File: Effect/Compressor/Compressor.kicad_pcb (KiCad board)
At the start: 2 copper layers, 30 x 62 mm, 34 parts, among them J1 Conn_01x04_Pin, J2 Conn_01x04_Pin, Q1 MMBF5103, Q2 DMMT5551, Q3 MMBF5103

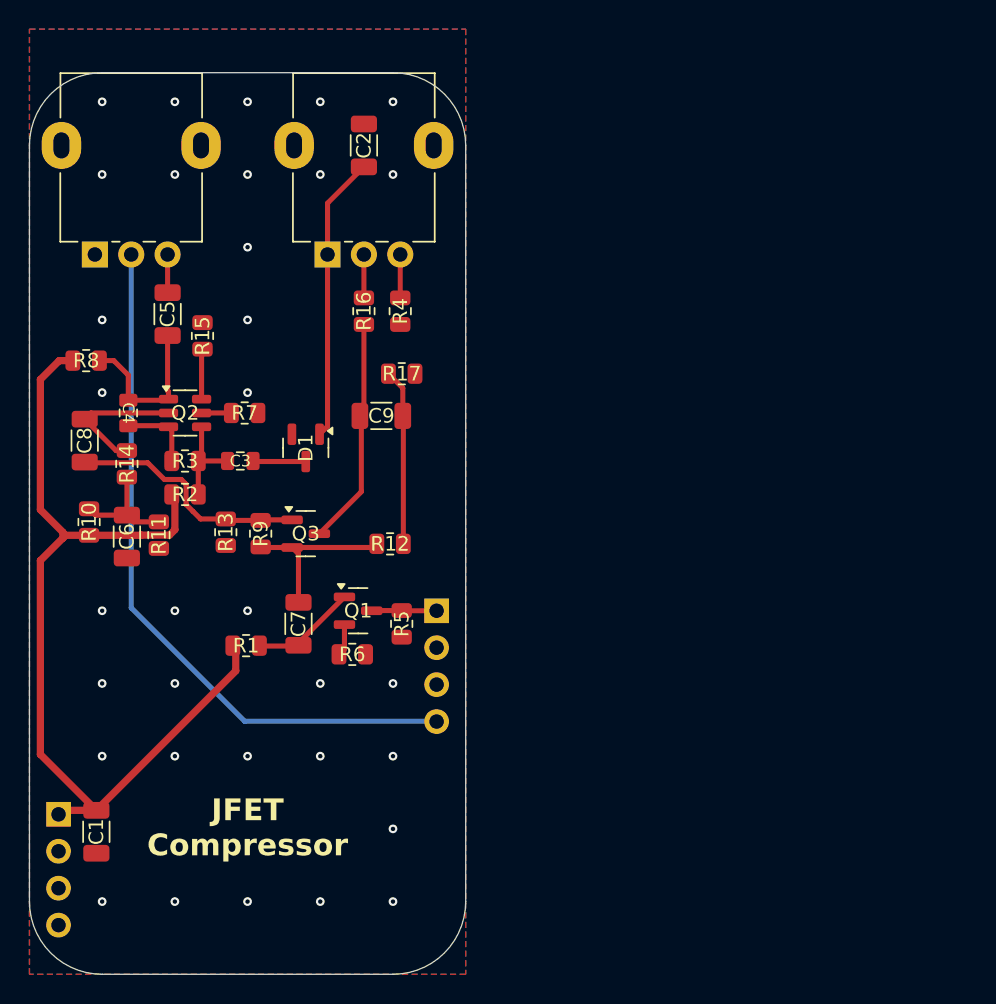
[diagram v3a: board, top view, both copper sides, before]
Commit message: More compressor updates: add pots for attack / decay tuning etc
Lots of minor changes, but the user-visible one is that there is
(limited) control of the attack and delay now.  But the whole compressor
level setup has also changed, and the signal amplification is done a bit
differently too using the NPN/PNP pair in the NMB2227A.

Can you say "trying out random things"? I knew you could.

Let's get this manufactured and see if it actually works, since I won't
have time to mess with the design any more as the merge window opens and
my travel season starts.

Signed-off-by: Linus Torvalds <torvalds@linux-foundation.org>
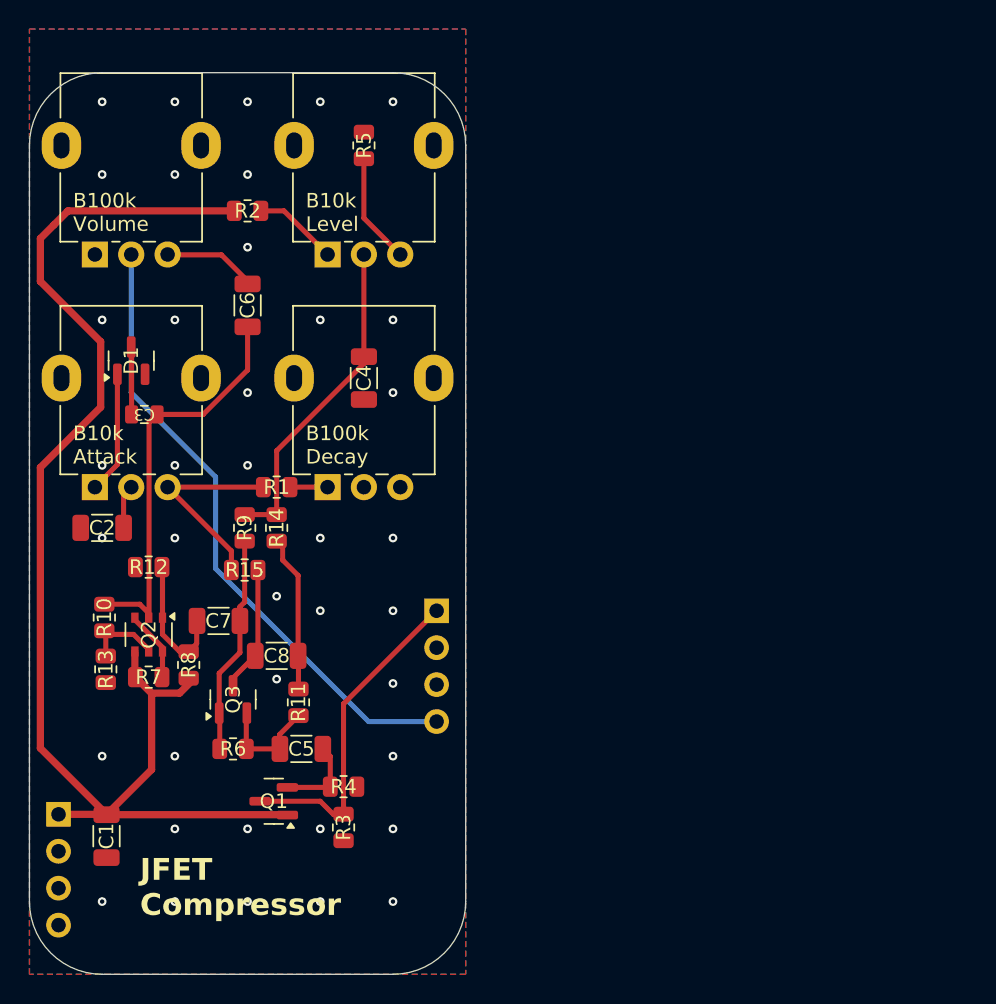
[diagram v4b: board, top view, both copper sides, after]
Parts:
- removed the C6 at (91.7, 94.9)
- removed the R11 at (93.9, 94.8)
- removed the R14 at (91.7, 89.9)
- removed the R3 at (95.7, 89.7)
- removed the R4 at (110.5, 79.4)
- removed the R8 at (88.9, 82.8)
- added R10: 2k2, Resistor_SMD:R_0805_2012Metric, F.Cu at (90.2, 100.5)
- added R12: 10k, Resistor_SMD:R_0805_2012Metric, F.Cu at (93.2, 97.0)
- added R5: 2k2, Resistor_SMD:R_0805_2012Metric, F.Cu at (108.0, 68.0)
- added RV2: 100k Decay, Mylib:Potentiometer_9mm_MP, F.Cu at (108.0, 84.0)
- added RV3: 10k Level, Mylib:Potentiometer_9mm_MP, F.Cu at (108.0, 68.0)
- C2: value 1uF -> 0.22uF
- C4: value 0.1uF -> 22uF; footprint Mylib:C_0704_1810Metric -> Capacitor_SMD:C_1206_3216Metric
- C5: renamed from C7; value 1uF -> 4.7uF
- C6: renamed from C5; value 1uF -> 4.7uF
- C7: renamed from C8; value 1uF -> 4.7uF
- Q2: value DMMT5551 -> NMB2227A; footprint Package_TO_SOT_SMD:SOT-23-6 -> Package_SO:TSOP-6_1.65x3.05mm_P0.95mm
- R1: value 1k5 -> 100k
- R13: renamed from R15; value 3k3 -> 1k
- R2: value 10k -> 33k
- R4: renamed from R6; value 1k -> 2k2
- R6: renamed from R9; value 33k -> 180k
- R7: value 3k3 -> 620
- R8: renamed from R10; value 100k -> 39k
- RV1: value 100k -> 10k Attack
- RV4: renamed from RV2; value 100k -> 100k Volume
- moved C2 31.9 mm to (90.0, 94.3), turned to 180 degrees
- moved R13 23.9 mm to (90.2, 104.0), turned to -90 degrees
- moved RV1 22.6 mm to (92.0, 84.0)
- moved R2 20.0 mm to (100.0, 72.5), turned to 180 degrees
- moved R15 19.6 mm to (99.8, 97.2), turned to 0 degrees
- moved R7 19.3 mm to (93.2, 104.6)
- moved C8 18.0 mm to (102.0, 103.1)
- moved C4 16.4 mm to (108.0, 84.0)
- moved Q2 15.4 mm to (93.2, 101.6), turned to -90 degrees
- moved C7 15.4 mm to (98.0, 100.7), turned to 180 degrees
- moved R6 14.9 mm to (99.0, 109.5), turned to 180 degrees
- moved R3 14.6 mm to (106.6, 114.9)
- moved Q1 14.3 mm to (101.8, 113.1), turned to 180 degrees
- moved R14 13.6 mm to (102.0, 94.3), turned to 90 degrees
- moved D1 13.4 mm to (92.0, 82.8), turned to 90 degrees
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- renumbered C9 to C8, R12 to R11, R17 to R14, R16 to R15, R5 to R3, R13 to R9
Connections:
- net Net-(Q3-D) renamed AMP_IN
- C2 pad 1: RECT -> Net-(C2-Pad1)
- C3 pad 1: Net-(Q2B-C) -> AMP_OUT
- C4 pad 1: FB -> LEVEL
- C4 pad 2: Net-(Q2B-B) -> GND
- C6 pad 1: FB -> AMP_OUT
- C7 pad 2: Net-(Q2A-B) -> Net-(Q2A-B1)
- D1 pad 1: RECT -> Net-(D1-A)
- Q1 pad 1: BUF_IN -> +V
- Q1 pad 2: Net-(Q1-S) -> BUF_IN
- Q2 pad 1: FB -> Net-(Q2A-B1)
- Q2 pad 2: Net-(Q2A-B) -> AMP_OUT
- Q2 pad 3: Net-(Q2B-B) -> Net-(Q2A-C1)
- Q2 pad 4: Net-(Q2B-C) -> +V
- Q2 pad 5: Net-(Q2B-E) -> Net-(Q2A-E1)
- Q2 pad 6: Net-(Q2A-E) -> Net-(Q2A-C1)
- R1 pad 1: +V -> Net-(R1-Pad1)
- R1 pad 2: BUF_IN -> RECT
- R13 pad 1: Net-(Q2A-E) -> Net-(Q2A-E1)
- R14 pad 2: GND -> LEVEL
- R15 pad 1: CONTROL -> RECT
- R2 pad 1: +V -> Net-(R2-Pad1)
- R2 pad 2: Net-(Q2B-C) -> +V
- R4 pad 1: Net-(Q1-S) -> BUF_IN
- R7 pad 1: Net-(Q2B-E) -> +V
- R7 pad 2: GND -> Net-(Q2A-C1)
- R8 pad 1: VBIAS -> Net-(Q2A-B1)
- R9 pad 2: GND -> LEVEL
- RV1 pad 1: RECT -> Net-(D1-A)
- RV1 pad 2: CONTROL -> Net-(C2-Pad1)
- RV1 pad 3: Net-(R4-Pad2) -> RECT
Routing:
- net AMP_OUT: track 0.00 -> 28.2 mm
- net +V: track 63.8 -> 91.1 mm
- net LEVEL: track 0.00 -> 22.6 mm
- net IN: track 4.47 -> 22.8 mm
- net FB: track 11.3 -> 0.00 mm
- net Net-(Q2A-B): track 9.73 -> 0.00 mm
- net Net-(Q2A-B1): track 0.00 -> 9.39 mm
- net Net-(D1-A): track 0.00 -> 8.40 mm
- net VBIAS: track 7.79 -> 0.00 mm
- net Net-(R5-Pad2): track 0.00 -> 7.62 mm
- net Net-(Q3-G): track 15.7 -> 8.67 mm
- net Net-(Q2B-C): track 6.76 -> 0.00 mm
- net Net-(R2-Pad1): track 0.00 -> 5.83 mm
- net RECT: track 19.7 -> 14.1 mm
- net Net-(Q2A-E1): track 0.00 -> 5.36 mm
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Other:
- board text added: "B100k Decay"
- board text added: "B100k Volume"
- board text added: "B10k Attack"
- board text added: "B10k Level"

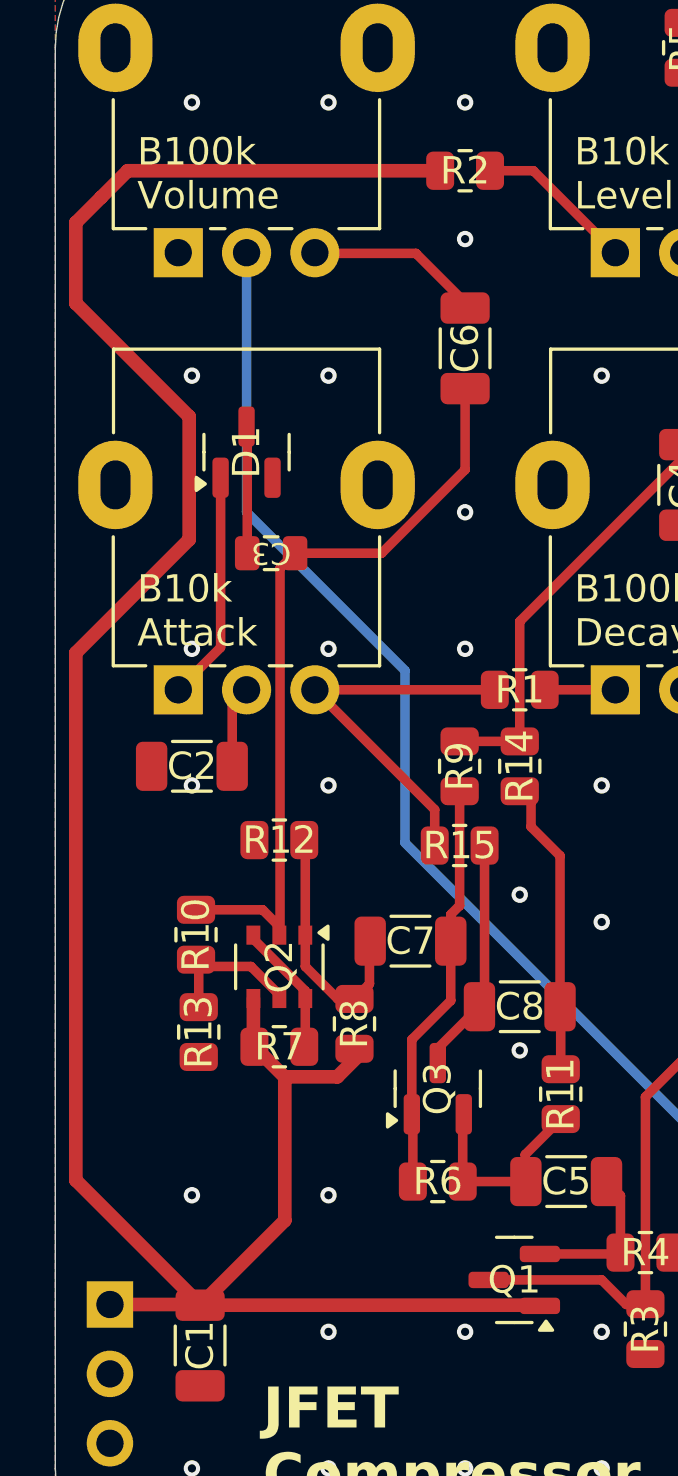
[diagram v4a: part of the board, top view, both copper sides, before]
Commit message: Gaah - Fix stupid PNP direction mistake
I've done this *so* many times: I turn the PNP around by rotating it
like it's some random resistor, not my mirroring it around the Y-axis,
and I end up with the transistor the wrong way around without noticing
it.

And I did it *again*.

It didn't actually seem to matter for simulation, because this whole
"use a series pair" was just for the lulz and there wasn't any big
current or voltage gain expected.  And so the single NPN was perfectly
happy to drive it all.

But it's still very wrong indeed.

This just fixes the direction of the transistor, but I'll go look closer
if it had some unfortunate effect on the rest of my flawed results.

Signed-off-by: Linus Torvalds <torvalds@linux-foundation.org>
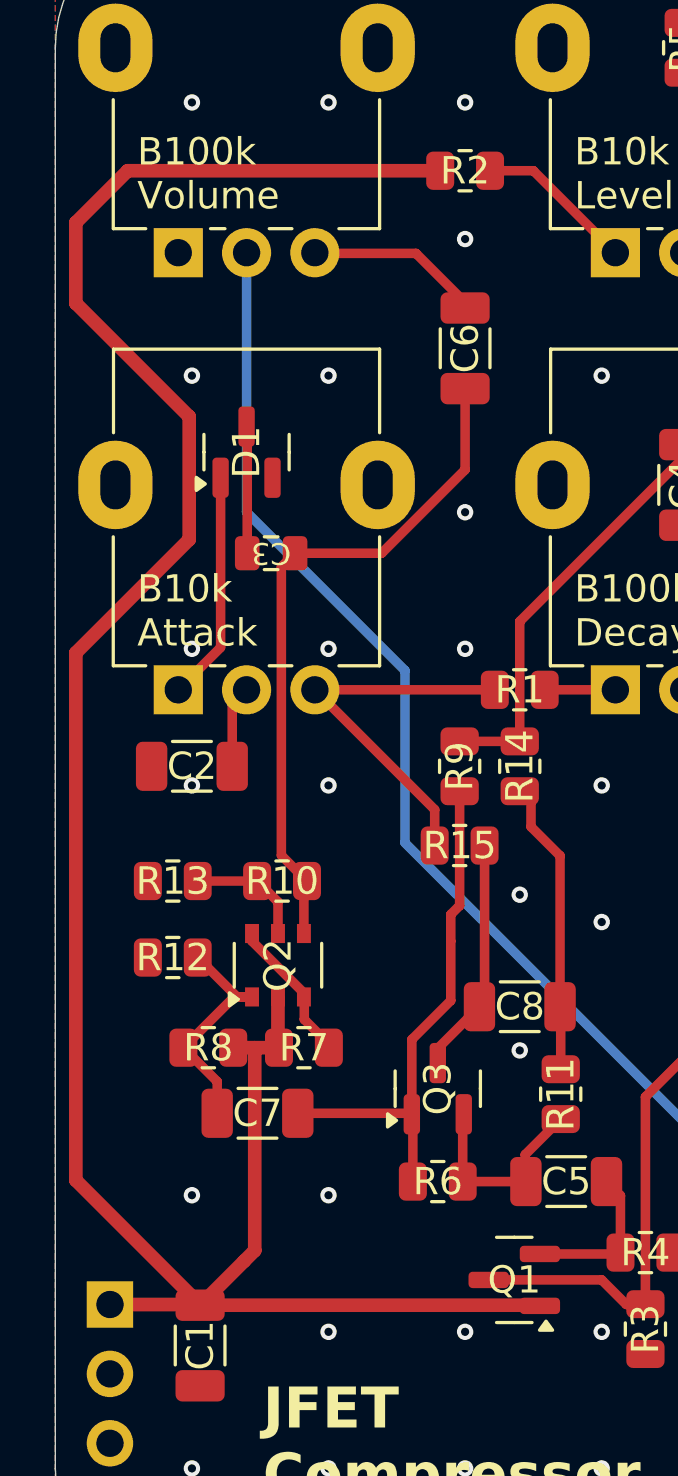
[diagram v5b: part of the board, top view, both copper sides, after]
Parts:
- moved C7 8.43 mm to (92.4, 107.0)
- moved R12 5.81 mm to (89.3, 101.3)
- moved R13 5.61 mm to (89.3, 98.5), turned to 180 degrees
- moved R8 5.42 mm to (90.6, 104.6), turned to 0 degrees
- moved R10 3.71 mm to (93.3, 98.5), turned to 180 degrees
- moved R7 0.90 mm to (94.1, 104.6)
- moved Q2 0.08 mm to (93.2, 101.6), turned to 90 degrees
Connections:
- Q2 pad 2: AMP_OUT -> +V
- Q2 pad 4: +V -> AMP_OUT
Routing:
- net AMP_IN: track 15.0 -> 19.2 mm
- net AMP_OUT: track 28.2 -> 25.0 mm
- net +V: track 91.1 -> 88.6 mm
- net Net-(Q2A-E1): track 5.36 -> 4.41 mm
- net Net-(Q2A-B1): track 9.39 -> 8.78 mm

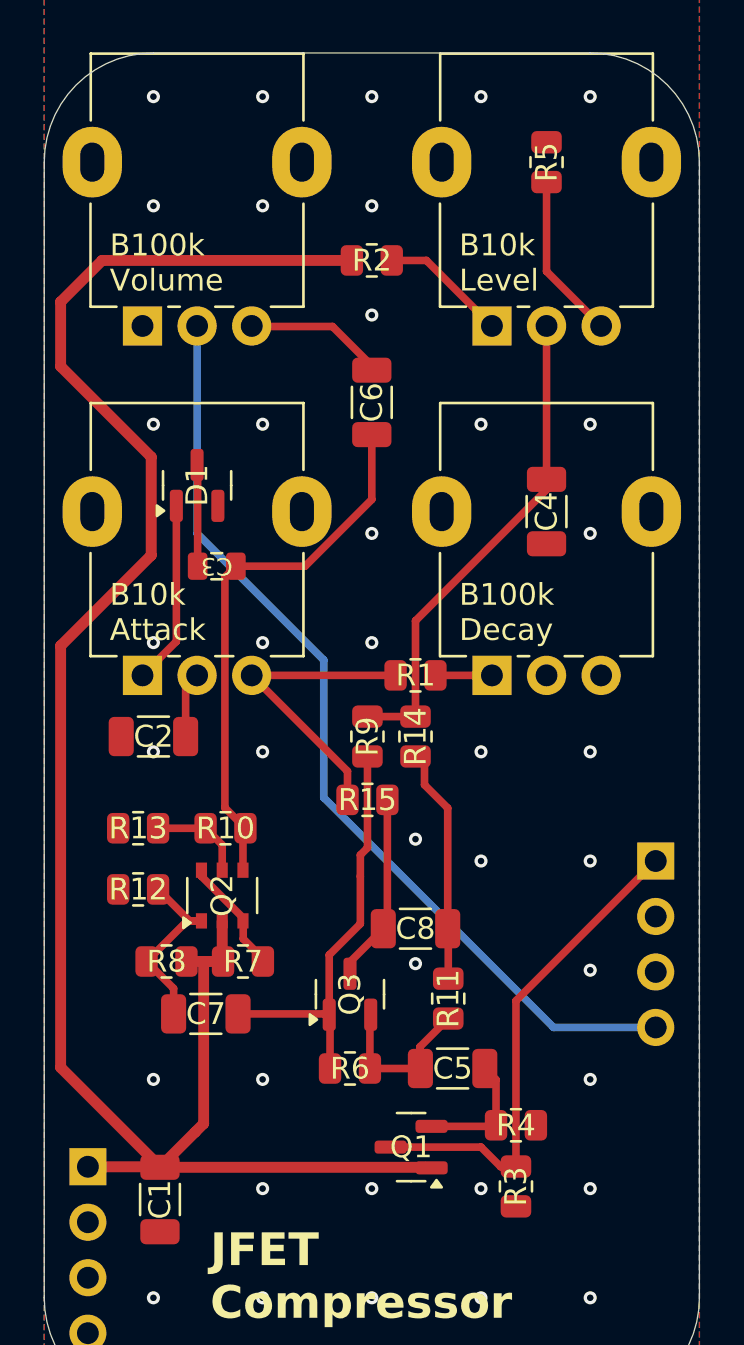
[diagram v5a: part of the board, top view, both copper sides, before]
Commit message: More compressor games
It turns ou tthat using the JFET to pass the signal (that I was so happy
about in commit c25f662: "Compressor: re-do with feedback loop and a
whole new approach") isn't so great after all.

In particular, it causes a kind of "zero-crossing distortion" where it
does compress the signal, but it does so by mainly compressing the
middle part, not the high ends.  Which looks all kinds of bad and
probably sounds worse.

I'm not 100% sure of the reason (I suspect there's some V_{DS} drop
effect), but clearly my clever trick was anything but.

Anyway, I do feel like I'm understanding how the JFET works much better
now, and I went back to the model with the JFET pulling the signal down,
and with my new-found understanding (famous last words) that looks a lot
better.

The whole "use a pot to set the voltage level" ended up making that
approach simpler too, because we don't now have to amplify the signal to
get that negative voltage with a diode/capacitor voltage inverter thing.
We can just adjust the level upwards to get a bigger V_{GS} drop..

This still does obviously amplify the signal, because we obviously don't
want to have a compressor that only makes the signal overall quieter.

I really would like to have a LED that shows when we start actually
compressing, but I'm still thinking about how to do that reasonably.

Signed-off-by: Linus Torvalds <torvalds@linux-foundation.org>
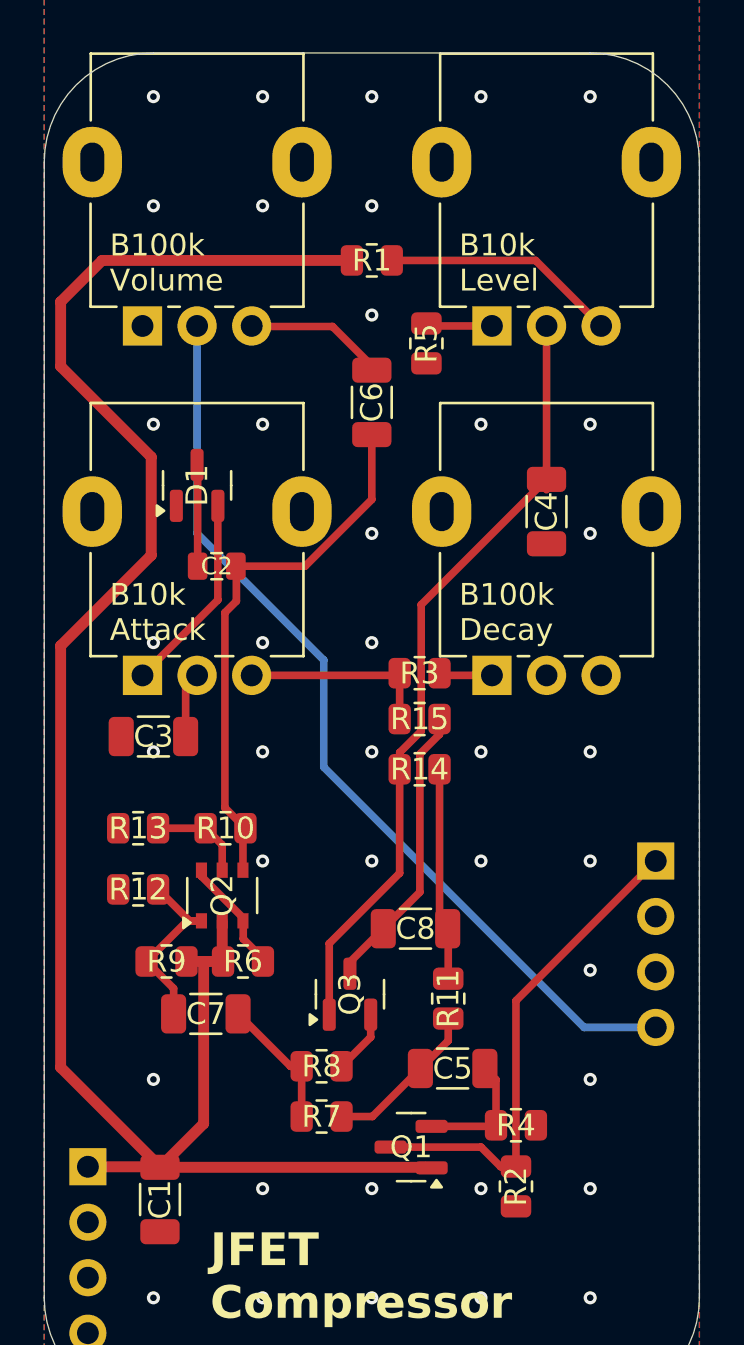
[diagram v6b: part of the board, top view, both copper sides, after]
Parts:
- removed the R6 at (99.0, 109.5)
- removed the R9 at (99.8, 94.3)
- added R7: 1k, Resistor_SMD:R_0805_2012Metric, F.Cu at (97.7, 111.7)
- added R8: 1k, Resistor_SMD:R_0805_2012Metric, F.Cu at (97.7, 109.4)
- C3: renamed from C2; value 0.22uF -> 0.47uF
- R5: value 2k2 -> 10k
- R9: renamed from R8; value 39k -> 33k
- moved R5 9.96 mm to (102.5, 76.3), turned to 90 degrees
- moved R15 4.40 mm to (102.2, 93.5)
- moved R14 1.51 mm to (102.2, 95.8), turned to 180 degrees
- moved R3 0.21 mm to (102.2, 91.4)
- renumbered C3 to C2, R2 to R1, R3 to R2, R1 to R3, R7 to R6, RV3 to RV2, RV2 to RV3
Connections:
- C5 pad 2: Net-(Q3-S) -> Net-(C5-Pad2)
- D1 pad 1: Net-(D1-A) -> GND
- D1 pad 2: GND -> Net-(D1-K)
- Q3 pad 1: AMP_IN -> LEVEL
- R1 pad 1: Net-(R2-Pad1) -> Net-(R1-Pad1)
- R11 pad 1: Net-(Q3-S) -> Net-(C5-Pad2)
- RV1 pad 1: Net-(D1-A) -> Net-(D1-K)
- RV2 pad 1: Net-(R2-Pad1) -> Net-(R5-Pad2)
- RV2 pad 3: Net-(R5-Pad2) -> Net-(R1-Pad1)
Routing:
- net LEVEL: track 22.6 -> 36.1 mm
- net AMP_IN: track 19.2 -> 6.21 mm
- net Net-(R1-Pad1): track 0.00 -> 10.8 mm
- net Net-(D1-K): track 0.00 -> 9.19 mm
- net Net-(D1-A): track 8.40 -> 0.00 mm
- net Net-(C5-Pad2): track 0.00 -> 7.34 mm
- net Net-(R2-Pad1): track 5.83 -> 0.00 mm
- net RECT: track 14.1 -> 8.49 mm
- net Net-(Q3-G): track 8.67 -> 14.1 mm
- net Net-(Q3-S): track 7.63 -> 2.92 mm
- net Net-(R5-Pad2): track 7.62 -> 3.05 mm
- net Net-(C8-Pad1): track 10.8 -> 9.72 mm
- net OUT: track 43.6 -> 42.7 mm
